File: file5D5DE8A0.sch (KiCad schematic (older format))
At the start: 10 parts, among them J3 Screw_Terminal_01x02, J4 Screw_Terminal_01x02, Q1 2N7002, Q2 2N7002, U4 JRC-21(4100), U5 JRC-21(4100)

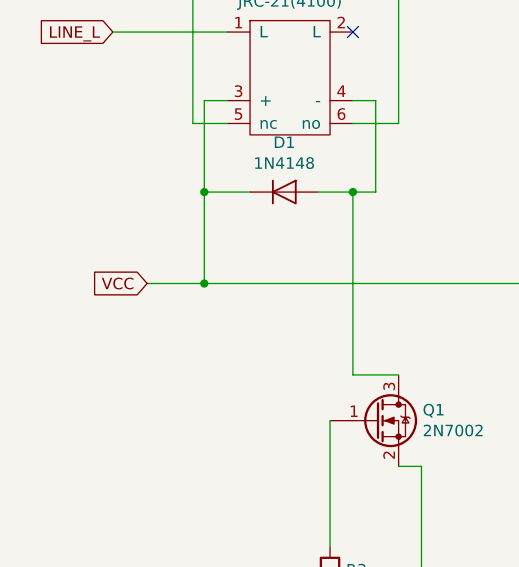
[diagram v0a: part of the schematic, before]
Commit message: regulador voltaje 3v3
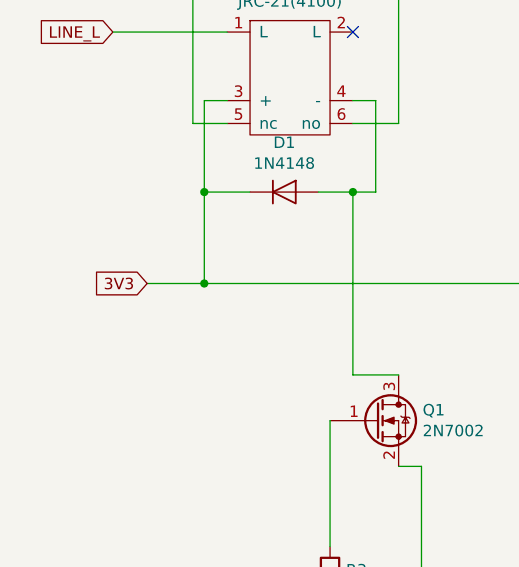
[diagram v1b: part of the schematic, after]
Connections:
- net VCC renamed 3V3
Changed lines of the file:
@@
 NoConn ~ 6050 2100
 NoConn ~ 6600 2100
-Text GLabel 4250 3150 0    50   Input ~ 0
-VCC
 Wire Wire Line
 	4250 3150 4500 3150
 Connection ~ 4500 3150
+Text GLabel 4250 3150 0    50   Input ~ 0
+3V3
 $EndSCHEMATC
